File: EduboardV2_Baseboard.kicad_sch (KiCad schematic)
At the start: 0 parts

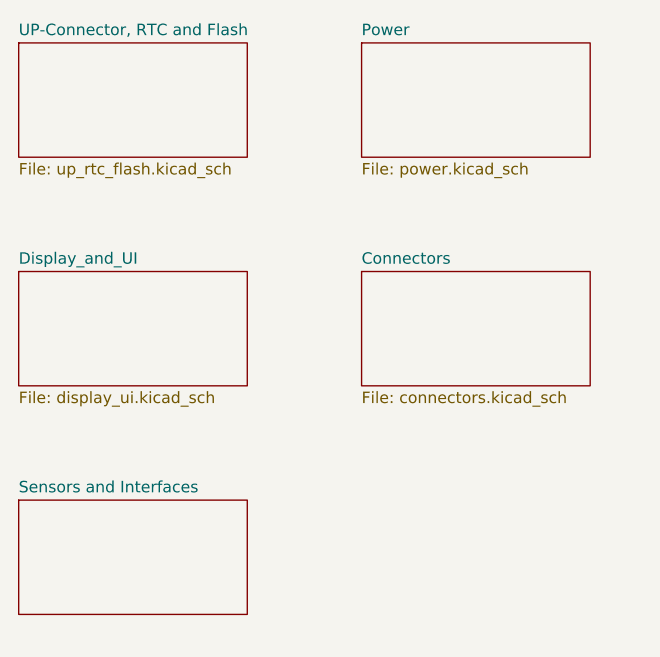
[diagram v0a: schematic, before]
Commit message: Add new Page for USB Hub circuit.
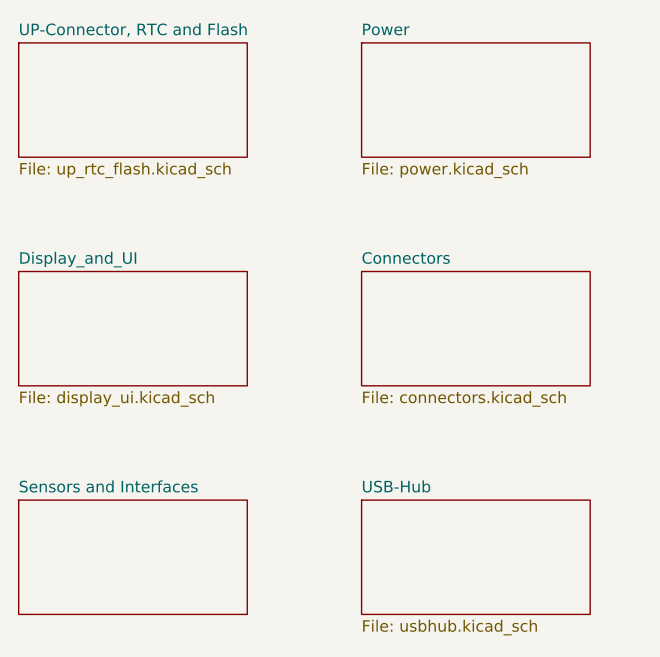
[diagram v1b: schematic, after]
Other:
- added sheet USB-Hub (usbhub.kicad_sch)
